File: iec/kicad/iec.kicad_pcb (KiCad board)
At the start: 2 copper layers, 48.1 x 34 mm, 7 parts, among them J1 Conn_RIOT, J2 RESET, J3 DIN-6, U1 74LS06

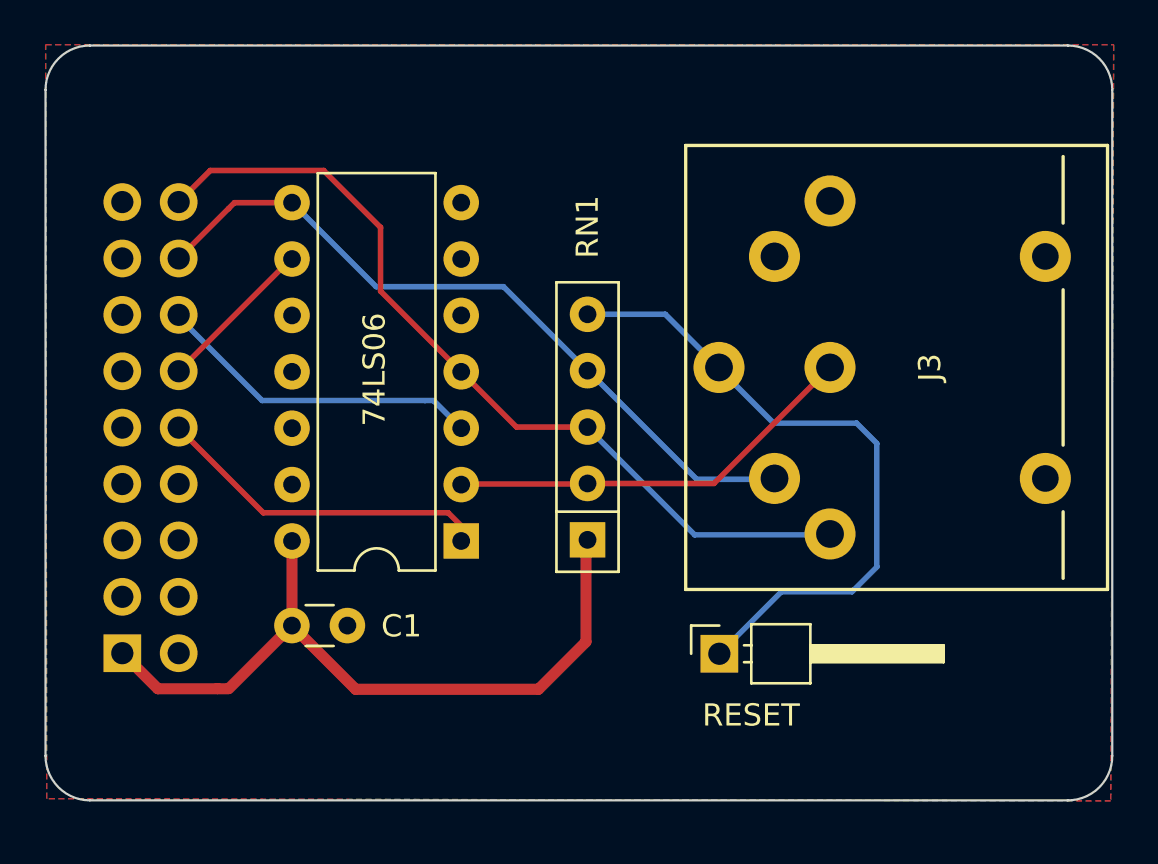
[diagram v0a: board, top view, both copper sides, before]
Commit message: Expose VCC and GND via pins for SD2IEC devices
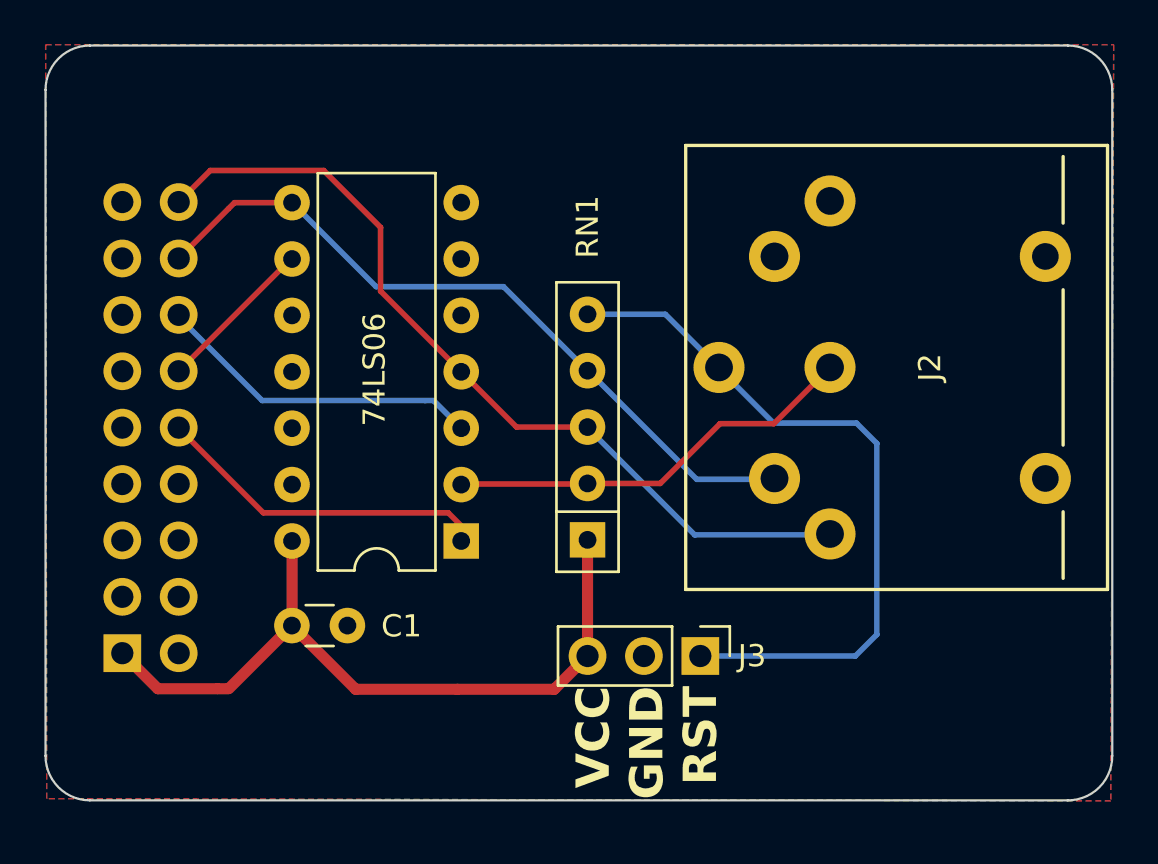
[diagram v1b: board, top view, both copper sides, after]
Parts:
- removed the J2 at (187.8, 110.9)
- added J3: Conn_Ext, Connector_PinHeader_2.54mm:PinHeader_1x03_P2.54mm_Vertical, F.Cu at (186.9, 111.0)
- renumbered J3 to J2
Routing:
- net ~{RESET}: track 29.7 -> 32.4 mm
- net VCC: track 32.7 -> 33.6 mm
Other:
- board text added: "VCC GND RST"
